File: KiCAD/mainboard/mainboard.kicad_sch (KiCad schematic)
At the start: 0 parts

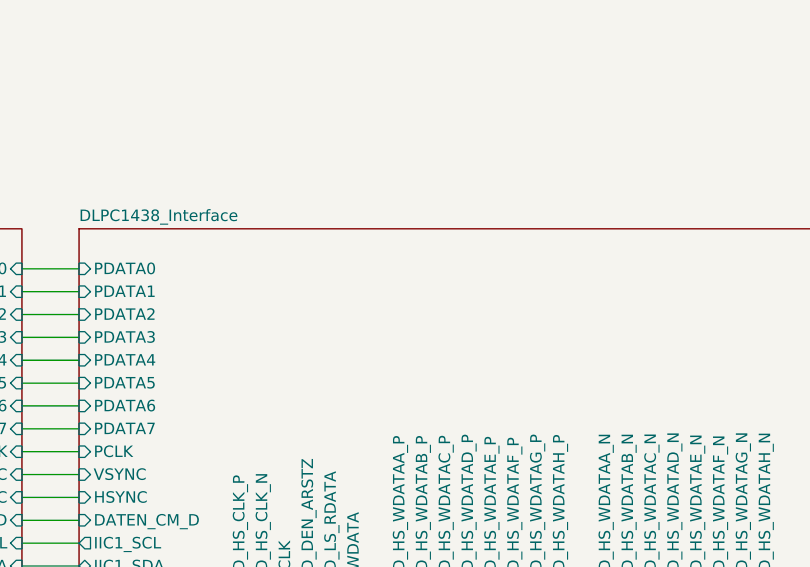
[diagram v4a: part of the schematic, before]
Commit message: designator names fixed
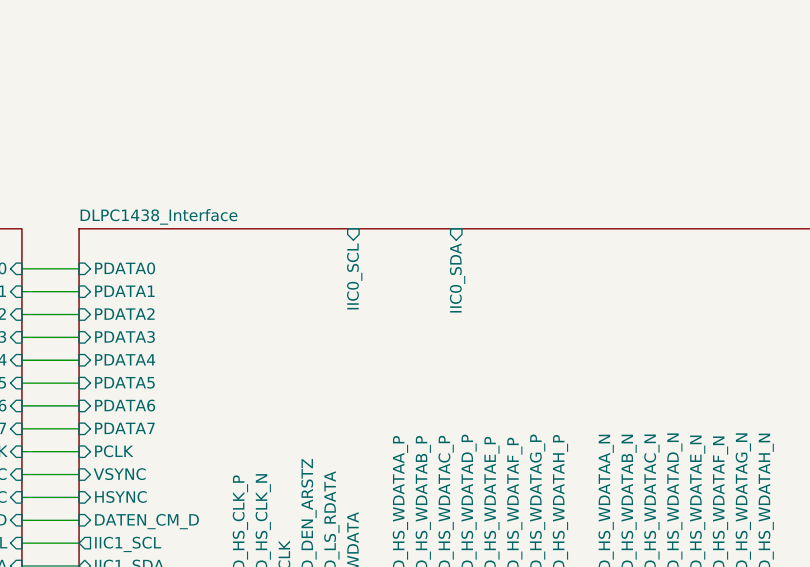
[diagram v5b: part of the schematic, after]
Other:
- sheet DLPC1438_Interface ports: added IIC0_SCL, IIC0_SDA; removed none
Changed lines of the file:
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@@
+			)
+		)
+		(pin "IIC0_SCL" input
+			(at 146.05 122.555 90)
+			(effects
+				(font
+					(size 1.27 1.27)
+				)
+				(justify right)
+			)
+		)
+		(pin "IIC0_SDA" input
+			(at 157.48 122.555 90)
+			(effects
+				(font
+					(size 1.27 1.27)
+				)
+				(justify right)
 			)
 		)

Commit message: more ERC knocked out
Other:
- sheet DLPA2005_Interface ports: added CMP_OUT, INTZ, LED_SEL_1, PROJ_ON, RC_CHARGE, SPI1_CLK, SPI1_CSZ0, SPI1_MISO, SPI1_MOSI; removed none
- sheet DLPC1438_Interface ports: added CMP_OUT, INTZ, LED_SEL_1, RESETZ; removed IIC0_SCL, IIC0_SDA
- sheet DMD_Interface ports: added none; removed SPI1_CLK, SPI1_CSZ0, SPI1_MISO, SPI1_MOSI
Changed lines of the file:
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@@
 	(wire
 		(pts
-			(xy 229.87 165.1) (xy 229.87 170.18)
+			(xy 247.65 132.08) (xy 252.73 132.08)
 		)
 		(stroke
@@
 	(wire
 		(pts
-			(xy 224.79 165.1) (xy 224.79 170.18)
-		)
-		(stroke
-			(width 0)
-			(type default)
-		)
-	)
-	(wire
-		(pts
 			(xy 109.22 149.86) (xy 115.57 149.86)
 		)
@@
 	(wire
 		(pts
+			(xy 247.65 154.94) (xy 252.73 154.94)
+		)
+		(stroke
+			(width 0)
+			(type default)
+		)
+	)
+	(wire
+		(pts
 			(xy 140.97 165.1) (xy 140.97 170.18)
 		)
@@
 	(wire
 		(pts
+			(xy 247.65 139.7) (xy 252.73 139.7)
+		)
+		(stroke
+			(width 0)
+			(type default)
+		)
+	)
+	(wire
+		(pts
 			(xy 135.89 165.1) (xy 135.89 170.18)
 		)
@@
 	(wire
 		(pts
+			(xy 247.65 135.89) (xy 252.73 135.89)
+		)
+		(stroke
+			(width 0)
+			(type default)
+		)
+	)
+	(wire
+		(pts
 			(xy 109.22 154.94) (xy 115.57 154.94)
 		)
@@
 	(wire
 		(pts
+			(xy 247.65 147.32) (xy 252.73 147.32)
+		)
+		(stroke
+			(width 0)
+			(type default)
+		)
+	)
+	(wire
+		(pts
+			(xy 247.65 124.46) (xy 252.73 124.46)
+		)
+		(stroke
+			(width 0)
+			(type default)
+		)
+	)
+	(wire
+		(pts
 			(xy 158.75 165.1) (xy 158.75 170.18)
 		)
@@
 	(wire
 		(pts
+			(xy 247.65 158.75) (xy 252.73 158.75)
+		)
+		(stroke
+			(width 0)
+			(type default)
+		)
+	)
+	(wire
+		(pts
 			(xy 156.21 165.1) (xy 156.21 170.18)
 		)
@@
 	(wire
 		(pts
+			(xy 252.73 162.56) (xy 247.65 162.56)
+		)
+		(stroke
+			(width 0)
+			(type default)
+		)
+	)
+	(wire
+		(pts
+			(xy 247.65 128.27) (xy 252.73 128.27)
+		)
+		(stroke
+			(width 0)
+			(type default)
+		)
+	)
+	(wire
+		(pts
 			(xy 184.15 165.1) (xy 184.15 170.18)
 		)
@@
 	(wire
 		(pts
-			(xy 227.33 165.1) (xy 227.33 170.18)
+			(xy 247.65 151.13) (xy 252.73 151.13)
 		)
 		(stroke
@@
 		(pts
 			(xy 173.99 165.1) (xy 173.99 170.18)
-		)
-		(stroke
-			(width 0)
-			(type default)
-		)
-	)
-	(wire
-		(pts
-			(xy 222.25 165.1) (xy 222.25 170.18)
 		)
 		(stroke
@@
 			)
 		)
-		(pin "SPI1_CLK" input
-			(at 222.25 170.18 90)
-			(effects
-				(font
-					(size 1.27 1.27)
-				)
-				(justify right)
-			)
-		)
-		(pin "SPI1_CSZ0" input
-			(at 224.79 170.18 90)
-			(effects
-				(font
-					(size 1.27 1.27)
-				)
-				(justify right)
-			)
-		)
-		(pin "SPI1_MISO" input
-			(at 227.33 170.18 90)
-			(effects
-				(font
-					(size 1.27 1.27)
-				)
-				(justify right)
-			)
-		)
-		(pin "SPI1_MOSI" input
-			(at 229.87 170.18 90)
-			(effects
-				(font
-					(size 1.27 1.27)
-				)
-				(justify right)
-			)
-		)
 		(instances
 			(project "mainboard"
@@
 		)
 		(pin "RESETZ" input
-			(at 252.73 125.73 180)
+			(at 252.73 128.27 180)
+			(effects
+				(font
+					(size 1.27 1.27)
+				)
+				(justify left)
+			)
+		)
+		(pin "CMP_OUT" input
+			(at 252.73 135.89 180)
+			(effects
+				(font
+					(size 1.27 1.27)
+				)
+				(justify left)
+			)
+		)
+		(pin "INTZ" input
+			(at 252.73 124.46 180)
+			(effects
+				(font
+					(size 1.27 1.27)
+				)
+				(justify left)
+			)
+		)
+		(pin "LED_SEL_1" input
+			(at 252.73 132.08 180)
+			(effects
+				(font
+					(size 1.27 1.27)
+				)
+				(justify left)
+			)
+		)
+		(pin "PROJ_ON" input
+			(at 252.73 147.32 180)
+			(effects
+				(font
+					(size 1.27 1.27)
+				)
+				(justify left)
+			)
+		)
+		(pin "RC_CHARGE" input
+			(at 252.73 139.7 180)
+			(effects
+				(font
+					(size 1.27 1.27)
+				)
+				(justify left)
+			)
+		)
+		(pin "SPI1_CLK" input
+			(at 252.73 154.94 180)
+			(effects
+				(font
+					(size 1.27 1.27)
+				)
+				(justify left)
+			)
+		)
+		(pin "SPI1_CSZ0" input
+			(at 252.73 162.56 180)
+			(effects
+				(font
+					(size 1.27 1.27)
+				)
+				(justify left)
+			)
+		)
+		(pin "SPI1_MISO" input
+			(at 252.73 158.75 180)
+			(effects
+				(font
+					(size 1.27 1.27)
+				)
+				(justify left)
+			)
+		)
+		(pin "SPI1_MOSI" input
+			(at 252.73 151.13 180)
 			(effects
 				(font
@@
 		)
 		(pin "FPGA_RDY" input
-			(at 247.65 147.32 0)
+			(at 157.48 122.555 90)
 			(effects
 				(font
@@
 		)
 		(pin "PROJ_ON" input
-			(at 247.65 152.4 0)
+			(at 247.65 147.32 0)
 			(effects
 				(font
@@
 		)
 		(pin "RC_CHARGE" input
-			(at 247.65 157.48 0)
+			(at 247.65 139.7 0)
 			(effects
 				(font
@@
 		)
 		(pin "THERM_PWR" input
-			(at 247.65 161.29 0)
+			(at 247.65 143.51 0)
 			(effects
 				(font
@@
 		)
 		(pin "ACT_SYNC" input
-			(at 247.65 142.24 0)
+			(at 161.29 122.555 90)
 			(effects
 				(font
@@
 		)
 		(pin "HOST_IR" input
-			(at 247.65 137.16 0)
+			(at 153.67 122.555 90)
 			(effects
 				(font
@@
 		)
 		(pin "SPI1_CLK" input
-			(at 222.25 165.1 270)
-			(effects
-				(font
-					(size 1.27 1.27)
-				)
-				(justify left)
+			(at 247.65 154.94 0)
+			(effects
+				(font
+					(size 1.27 1.27)
+				)
+				(justify right)
 			)
 		)
 		(pin "SPI1_CSZ0" input
-			(at 224.79 165.1 270)
-			(effects
-				(font
-					(size 1.27 1.27)
-				)
-				(justify left)
+			(at 247.65 162.56 0)
+			(effects
+				(font
+					(size 1.27 1.27)
+				)
+				(justify right)
 			)
 		)
 		(pin "SPI1_MISO" input
-			(at 227.33 165.1 270)
-			(effects
-				(font
-					(size 1.27 1.27)
-				)
-				(justify left)
+			(at 247.65 158.75 0)
+			(effects
+				(font
+					(size 1.27 1.27)
+				)
+				(justify right)
 			)
 		)
 		(pin "SPI1_MOSI" input
-			(at 229.87 165.1 270)
-			(effects
-				(font
-					(size 1.27 1.27)
-				)
-				(justify left)
-			)
-		)
-		(pin "IIC0_SCL" input
-			(at 146.05 122.555 90)
-			(effects
-				(font
-					(size 1.27 1.27)
-				)
-				(justify right)
-			)
-		)
-		(pin "IIC0_SDA" input
-			(at 157.48 122.555 90)
-			(effects
-				(font
+			(at 247.65 151.13 0)
+			(effects
+				(font
+					(size 1.27 1.27)
+				)
+				(justify right)
+			)
+		)
+		(pin "INTZ" input
+			(at 247.65 124.46 0)
+			(effects
+				(font
+					(size 1.27 1.27)
+				)
+				(justify right)
+			)
+		)
+		(pin "LED_SEL_1" input
+			(at 247.65 132.08 0)
+			(effects
+				(font
+					(size 1.27 1.27)
+				)
+				(justify right)
+			)
+		)
+		(pin "RESETZ" input
+			(at 247.65 128.27 0)
+			(effects
+				(font
+					(size 1.27 1.27)
+				)
+				(justify right)
+			)
+		)
+		(pin "CMP_OUT" input
+			(at 247.65 135.89 0)
+			(effects
+				(font

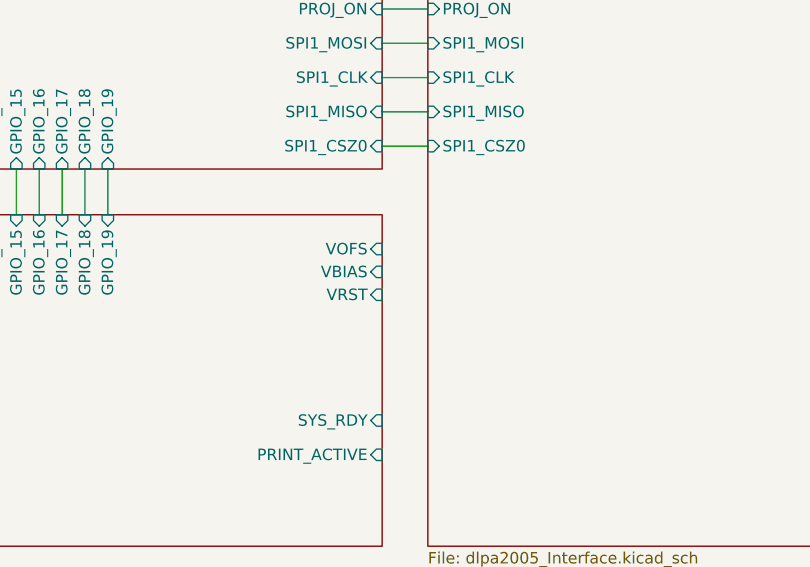
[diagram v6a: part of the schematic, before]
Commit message: meeting edits to DLPA and DLPC
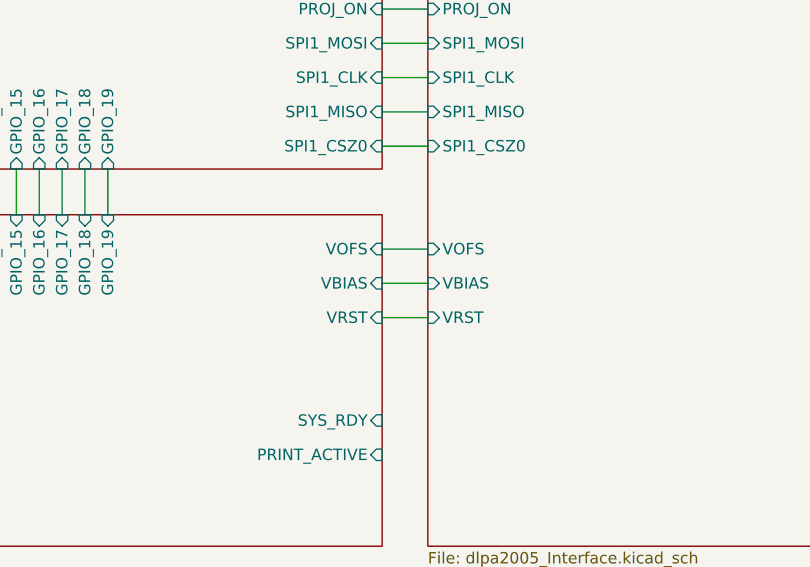
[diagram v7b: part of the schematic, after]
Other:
- sheet DLPA2005_Interface ports: added VBIAS, VOFS, VRST; removed none
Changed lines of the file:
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@@
+	(wire
+		(pts
+			(xy 247.65 173.99) (xy 252.73 173.99)
+		)
+		(stroke
+			(width 0)
+			(type default)
+		)
+	)
 	(wire
 		(pts
@@
 		(pts
 			(xy 247.65 147.32) (xy 252.73 147.32)
+		)
+		(stroke
+			(width 0)
+			(type default)
+		)
+	)
+	(wire
+		(pts
+			(xy 247.65 181.61) (xy 252.73 181.61)
+		)
+		(stroke
+			(width 0)
+			(type default)
+		)
+	)
+	(wire
+		(pts
+			(xy 247.65 177.8) (xy 252.73 177.8)
 		)
 		(stroke
@@
 		)
 		(pin "VBIAS" input
-			(at 247.65 176.53 0)
+			(at 247.65 177.8 0)
 			(effects
 				(font
@@
 		)
 		(pin "VRST" input
-			(at 247.65 179.07 0)
+			(at 247.65 181.61 0)
 			(effects
 				(font
@@
 			(effects
 				(font
+					(size 1.27 1.27)
+				)
+				(justify left)
+			)
+		)
+		(pin "VBIAS" input
+			(at 252.73 177.8 180)
+			(effects
+				(font
+					(size 1.27 1.27)
+				)
+				(justify left)
+			)
+		)
+		(pin "VOFS" input
+			(at 252.73 173.99 180)
+			(effects
+				(font
+					(size 1.27 1.27)
+				)
+				(justify left)
+			)
+		)
+		(pin "VRST" input
+			(at 252.73 181.61 180)
+			(effects
+				(font

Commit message: nothing to report
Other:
- sheet DLPC1438_Interface ports: added none; removed ACT_SYNC
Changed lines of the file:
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@@
-			)
-		)
-		(pin "ACT_SYNC" input
-			(at 161.29 122.555 90)
-			(effects
-				(font
-					(size 1.27 1.27)
-				)
-				(justify right)
 			)
 		)
